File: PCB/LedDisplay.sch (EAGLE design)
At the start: 32 parts, among them IC1 AT90S2313S, IC2 74164D, IC3 74164D, IC4 74164D

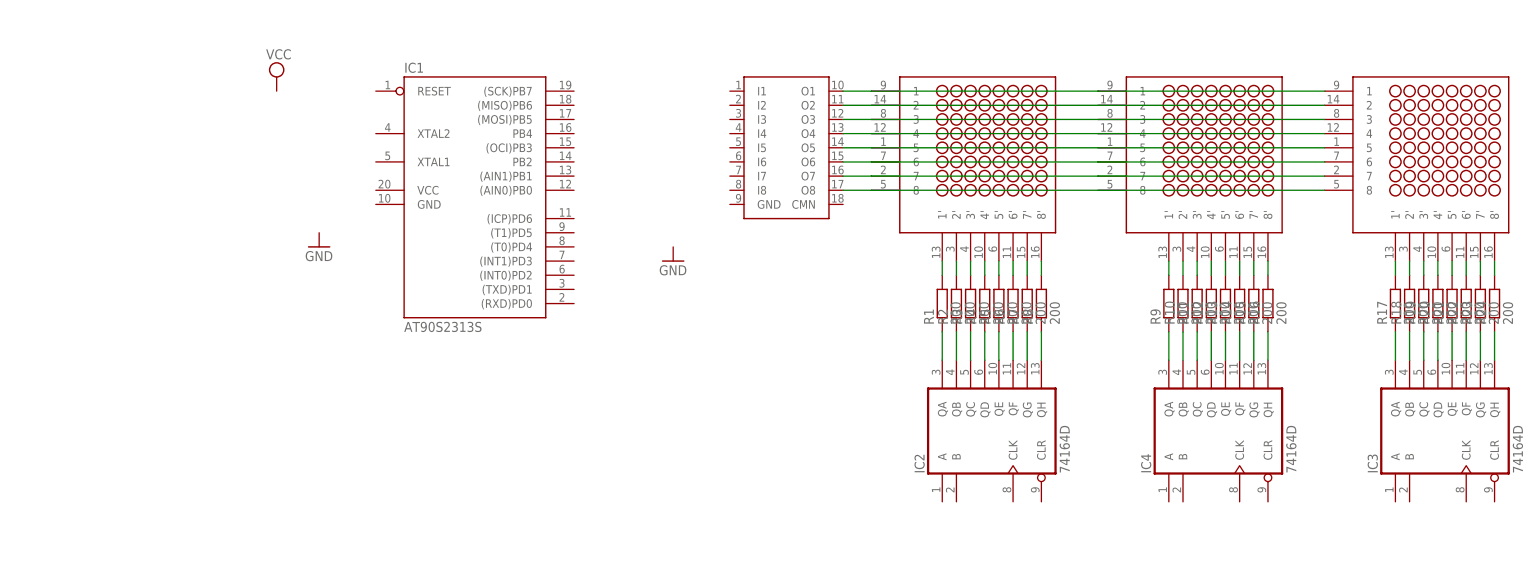
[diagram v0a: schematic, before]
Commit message: Updated pcb dimensions. Now is fits perfectly to the casing. Also some of the elements were changed to DIP packages.
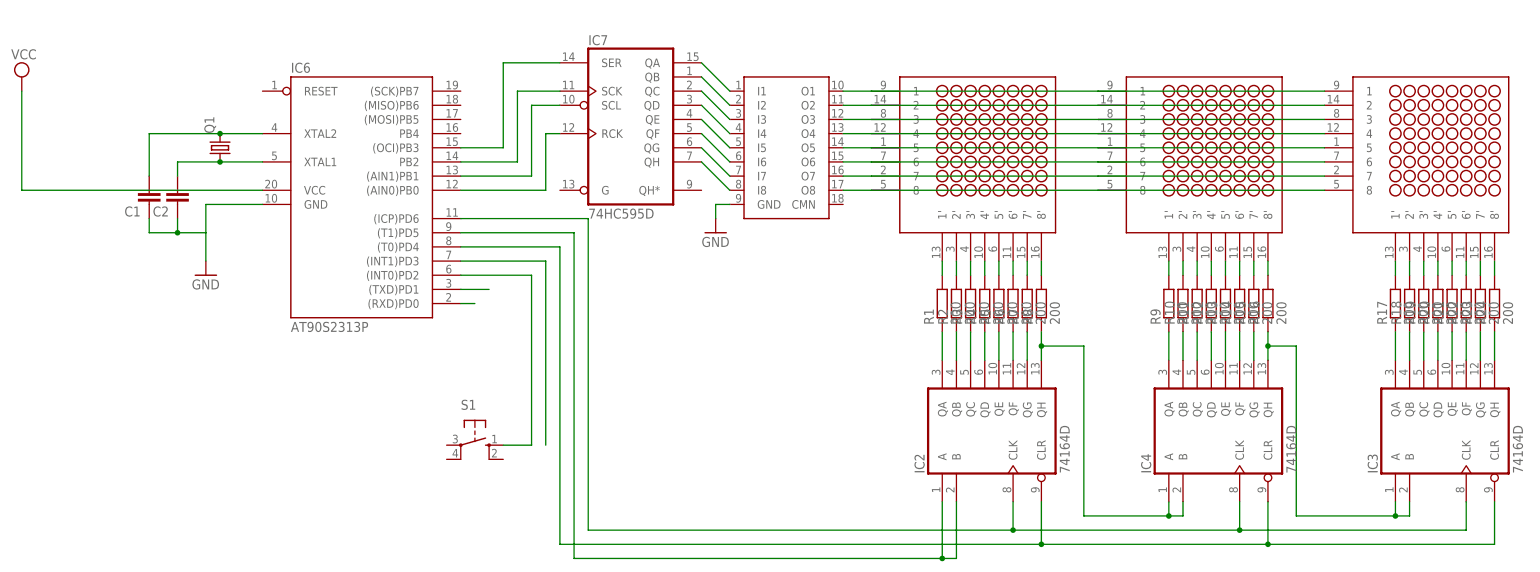
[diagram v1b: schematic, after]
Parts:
- removed IC1: AT90S2313S, atmel:AT90S2313S
- added C1, C2: (no value), capacitor-wima:C2,5-3
- added IC6: AT90S2313P, atmel:AT90S2313P
- added IC7: 74HC595D, 74xx-eu:74HC595D
- added Q1: (no value), crystal:CRYSTALHC49U70
- added S1: (no value), switch-omron:10-XX
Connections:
- new net GND: C1.1, C2.1, IC6.GND, U$4.GND
- new net N$1: IC7A.QH, U$4.I8
- new net N$2: IC7A.QG, U$4.I7
- new net N$3: IC7A.QF, U$4.I6
- new net N$4: IC7A.QE, U$4.I5
- new net N$5: IC7A.QD, U$4.I4
- new net N$57: C1.2, IC6.XTAL2, Q1.2
- new net N$58: C2.2, IC6.XTAL1, Q1.1
- new net N$59: IC6.(RXD)PD0
- new net N$6: IC7A.QC, U$4.I3
- new net N$60: IC6.(TXD)PD1
- new net N$61: IC2A.CLR, IC3A.CLR, IC4A.CLR, IC6.(T0)PD4
- new net N$62: IC2A.A, IC2A.B, IC6.(T1)PD5
- new net N$63: IC2A.CLK, IC3A.CLK, IC4A.CLK, IC6.(ICP)PD6
- new net N$64: IC6.(INT0)PD2, S1.S
- new net N$65: IC6.(INT1)PD3
- new net N$7: IC7A.QB, U$4.I2
- new net N$74: IC6.(AIN0)PB0, IC7A.RCK
- new net N$75: IC6.(AIN1)PB1, IC7A.SCL
- new net N$76: IC6.PB2, IC7A.SCK
- new net N$77: IC6.(OCI)PB3, IC7A.SER
- new net N$8: IC7A.QA, U$4.I1
- new net VCC: IC6.VCC
- net N$24: now also IC4A.A, IC4A.B
- net N$40: now also IC3A.A, IC3A.B

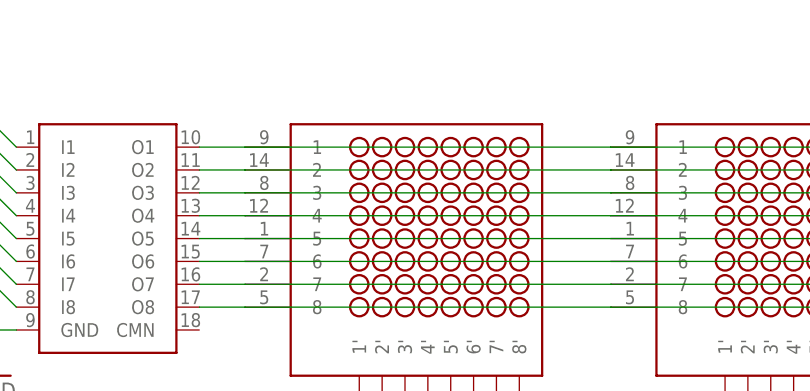
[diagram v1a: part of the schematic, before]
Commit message: Another part of improvements in pcb layout, especially on the top layer.
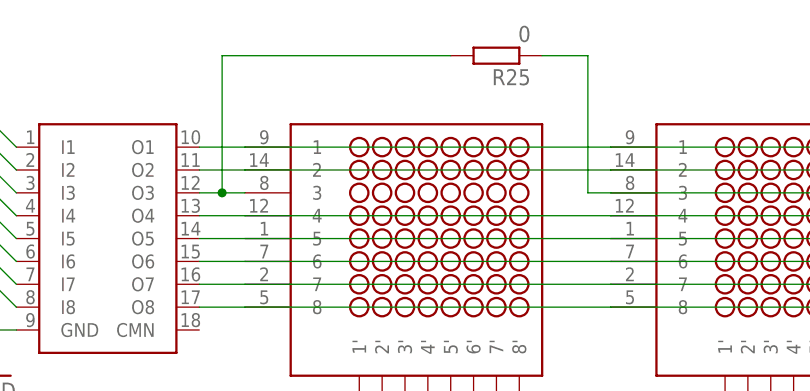
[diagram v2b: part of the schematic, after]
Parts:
- added R25: 0, resistor:R-EU_M1206
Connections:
- new net N$78: R25.2, U$1.3, U$4.O3
- net N$68: now also R25.1; no longer U$1.3, U$4.O3
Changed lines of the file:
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@@
 <grid distance="0.1" unitdist="inch" unit="inch" style="lines" multiple="1" display="no" altdistance="0.01" altunitdist="inch" altunit="inch"/>
 <layers>
-<layer number="1" name="Top" color="4" fill="1" visible="no" active="no"/>
-<layer number="16" name="Bottom" color="1" fill="1" visible="no" active="no"/>
-<layer number="17" name="Pads" color="2" fill="1" visible="no" active="no"/>
-<layer number="18" name="Vias" color="2" fill="1" visible="no" active="no"/>
-<layer number="19" name="Unrouted" color="6" fill="1" visible="no" active="no"/>
-<layer number="20" name="Dimension" color="15" fill="1" visible="no" active="no"/>
-<layer number="21" name="tPlace" color="7" fill="1" visible="no" active="no"/>
-<layer number="22" name="bPlace" color="7" fill="1" visible="no" active="no"/>
-<layer number="23" name="tOrigins" color="15" fill="1" visible="no" active="no"/>
-<layer number="24" name="bOrigins" color="15" fill="1" visible="no" active="no"/>
-<layer number="25" name="tNames" color="7" fill="1" visible="no" active="no"/>
-<layer number="26" name="bNames" color="7" fill="1" visible="no" active="no"/>
-<layer number="27" name="tValues" color="7" fill="1" visible="no" active="no"/>
-<layer number="28" name="bValues" color="7" fill="1" visible="no" active="no"/>
+<layer number="1" name="Top" color="4" fill="1" visible="yes" active="no"/>
+<layer number="16" name="Bottom" color="1" fill="1" visible="yes" active="no"/>
+<layer number="17" name="Pads" color="2" fill="1" visible="yes" active="no"/>
+<layer number="18" name="Vias" color="2" fill="1" visible="yes" active="no"/>
+<layer number="19" name="Unrouted" color="13" fill="1" visible="yes" active="no"/>
+<layer number="20" name="Dimension" color="15" fill="1" visible="yes" active="no"/>
+<layer number="21" name="tPlace" color="7" fill="1" visible="yes" active="no"/>
+<layer number="22" name="bPlace" color="7" fill="1" visible="yes" active="no"/>
+<layer number="23" name="tOrigins" color="15" fill="1" visible="yes" active="no"/>
+<layer number="24" name="bOrigins" color="15" fill="1" visible="yes" active="no"/>
+<layer number="25" name="tNames" color="7" fill="1" visible="yes" active="no"/>
+<layer number="26" name="bNames" color="7" fill="1" visible="yes" active="no"/>
+<layer number="27" name="tValues" color="7" fill="1" visible="yes" active="no"/>
+<layer number="28" name="bValues" color="7" fill="1" visible="yes" active="no"/>
 <layer number="29" name="tStop" color="7" fill="3" visible="no" active="no"/>
 <layer number="30" name="bStop" color="7" fill="6" visible="no" active="no"/>
@@
 <layer number="35" name="tGlue" color="7" fill="4" visible="no" active="no"/>
 <layer number="36" name="bGlue" color="7" fill="5" visible="no" active="no"/>
-<layer number="37" name="tTest" color="7" fill="1" visible="no" active="no"/>
-<layer number="38" name="bTest" color="7" fill="1" visible="no" active="no"/>
+<layer number="37" name="tTest" color="7" fill="1" visible="yes" active="no"/>
+<layer number="38" name="bTest" color="7" fill="1" visible="yes" active="no"/>
 <layer number="39" name="tKeepout" color="4" fill="11" visible="no" active="no"/>
 <layer number="40" name="bKeepout" color="1" fill="11" visible="no" active="no"/>
@@
 <layer number="44" name="Drills" color="7" fill="1" visible="no" active="no"/>
 <layer number="45" name="Holes" color="7" fill="1" visible="no" active="no"/>
-<layer number="46" name="Milling" color="3" fill="1" visible="no" active="no"/>
-<layer number="47" name="Measures" color="7" fill="1" visible="no" active="no"/>
-<layer number="48" name="Document" color="7" fill="1" visible="no" active="no"/>
-<layer number="49" name="Reference" color="7" fill="1" visible="no" active="no"/>
-<layer number="50" name="dxf" color="7" fill="1" visible="no" active="no"/>
-<layer number="51" name="tDocu" color="6" fill="9" visible="no" active="no"/>
-<layer number="52" name="bDocu" color="7" fill="1" visible="no" active="no"/>
-<layer number="53" name="tGND_GNDA" color="7" fill="9" visible="no" active="no"/>
-<layer number="54" name="bGND_GNDA" color="1" fill="9" visible="no" active="no"/>
-<layer number="56" name="wert" color="7" fill="1" visible="no" active="no"/>
+<layer number="46" name="Milling" color="3" fill="1" visible="yes" active="no"/>
+<layer number="47" name="Measures" color="7" fill="1" visible="yes" active="no"/>
+<layer number="48" name="Document" color="7" fill="1" visible="yes" active="no"/>
+<layer number="49" name="Reference" color="7" fill="1" visible="yes" active="no"/>
+<layer number="50" name="dxf" color="7" fill="1" visible="yes" active="no"/>
+<layer number="51" name="tDocu" color="7" fill="1" visible="yes" active="no"/>
+<layer number="52" name="bDocu" color="7" fill="1" visible="yes" active="no"/>
+<layer number="53" name="tGND_GNDA" color="7" fill="9" visible="yes" active="no"/>
+<layer number="54" name="bGND_GNDA" color="1" fill="9" visible="yes" active="no"/>
+<layer number="56" name="wert" color="7" fill="1" visible="yes" active="no"/>
 <layer number="91" name="Nets" color="2" fill="1" visible="yes" active="yes"/>
 <layer number="92" name="Busses" color="1" fill="1" visible="yes" active="yes"/>
@@
 <part name="IC7" library="74xx-eu" deviceset="74*595" device="D" technology="HC"/>
 <part name="U$4" library="MJ" deviceset="ULN2803A" device=""/>
+<part name="R25" library="resistor" deviceset="R-EU_" device="M1206" value="0"/>
 </parts>
 <sheets>
@@
 <instance part="IC7" gate="A" x="7.62" y="88.9"/>
 <instance part="U$4" gate="G$1" x="35.56" y="83.82"/>
+<instance part="R25" gate="G$1" x="78.74" y="104.14" rot="R180"/>
 </instances>
 <busses>
@@
 <net name="N$68" class="0">
 <segment>
-<pinref part="U$1" gate="G$1" pin="3"/>
 <pinref part="U$2" gate="G$1" pin="3"/>
-<wire x1="50.8" y1="88.9" x2="91.44" y2="88.9" width="0.1524" layer="91"/>
 <pinref part="U$3" gate="G$1" pin="3"/>
 <wire x1="91.44" y1="88.9" x2="132.08" y2="88.9" width="0.1524" layer="91"/>
-<pinref part="U$4" gate="G$1" pin="O3"/>
-<wire x1="50.8" y1="88.9" x2="45.72" y2="88.9" width="0.1524" layer="91"/>
+<wire x1="91.44" y1="88.9" x2="88.9" y2="88.9" width="0.1524" layer="91"/>
+<wire x1="88.9" y1="88.9" x2="88.9" y2="104.14" width="0.1524" layer="91"/>
+<pinref part="R25" gate="G$1" pin="1"/>
+<wire x1="88.9" y1="104.14" x2="83.82" y2="104.14" width="0.1524" layer="91"/>
 </segment>
 </net>
@@
 </segment>
 </net>
+<net name="N$78" class="0">
+<segment>
+<pinref part="U$4" gate="G$1" pin="O3"/>
+<pinref part="U$1" gate="G$1" pin="3"/>
+<wire x1="50.8" y1="88.9" x2="48.26" y2="88.9" width="0.1524" layer="91"/>
+<wire x1="48.26" y1="88.9" x2="45.72" y2="88.9" width="0.1524" layer="91"/>
+<wire x1="48.26" y1="88.9" x2="48.26" y2="104.14" width="0.1524" layer="91"/>
+<pinref part="R25" gate="G$1" pin="2"/>
+<wire x1="48.26" y1="104.14" x2="73.66" y2="104.14" width="0.1524" layer="91"/>
+<junction x="48.26" y="88.9"/>
+</segment>
+</net>
